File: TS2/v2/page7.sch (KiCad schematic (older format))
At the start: 10 parts, among them P1 FTDI (TERMINAL), P2 FTDI (HOST), U29 6850, U3 74LS00, U30 6850, U31 MC14411, U5 74LS04, Y1 1.842MHz

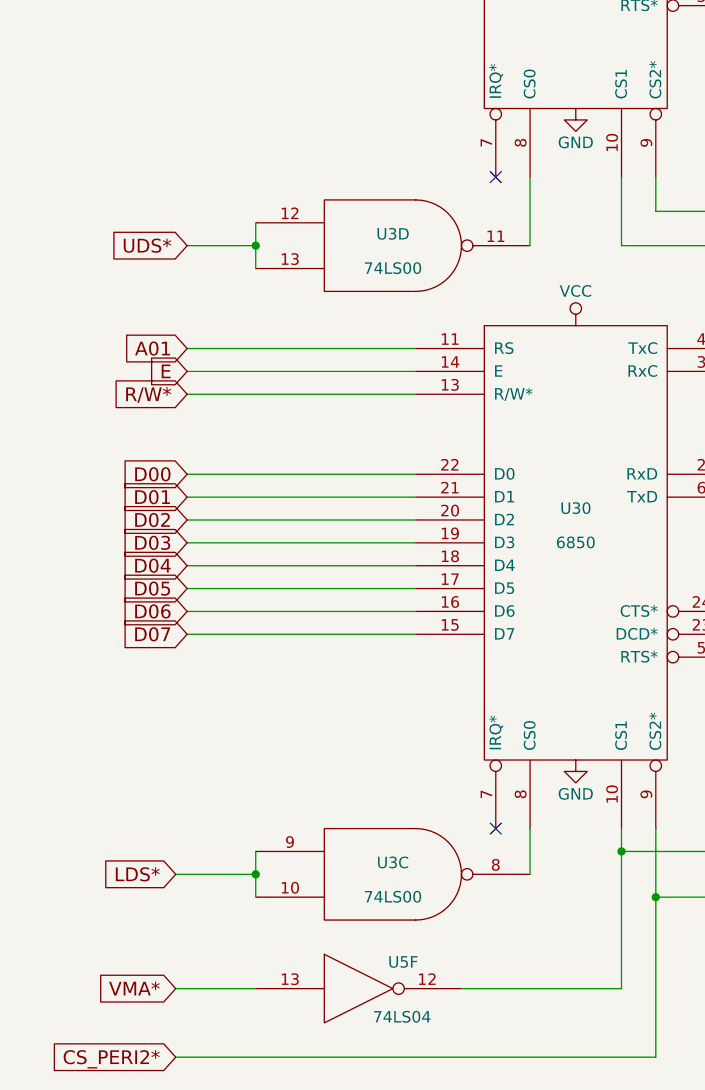
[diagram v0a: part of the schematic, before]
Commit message: Implementing more of interrupt circuitry.
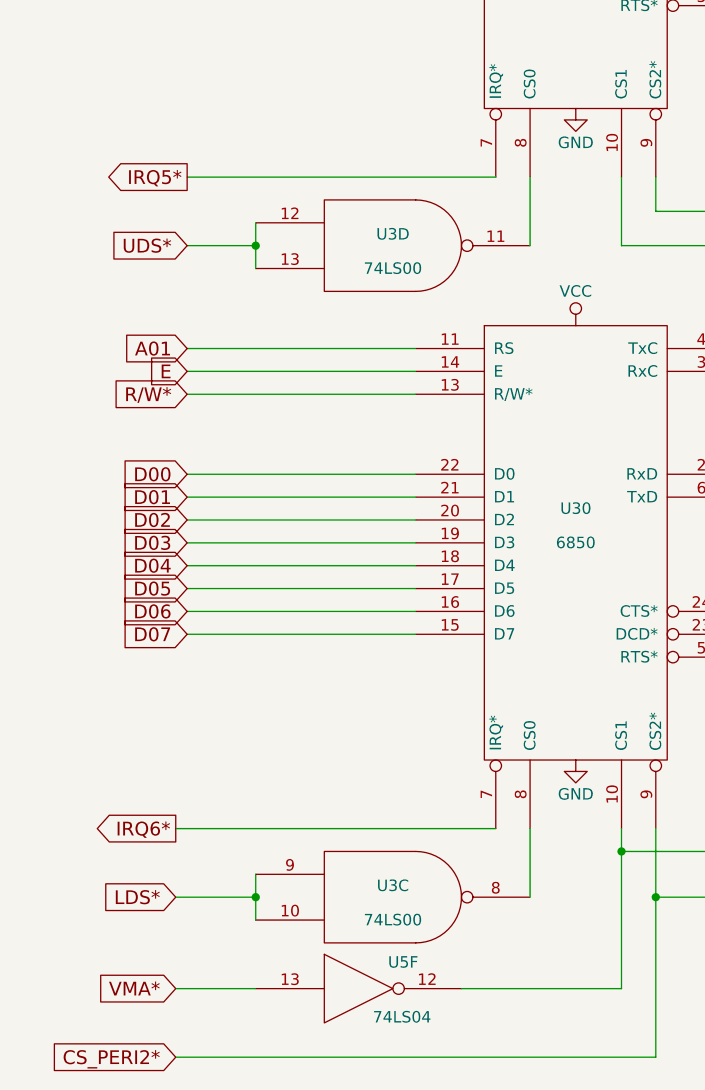
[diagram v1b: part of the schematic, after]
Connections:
- net IRQ5*: now reaches U29.7 (IRQ*)
- net IRQ6*: now reaches U30.7 (IRQ*)
- no-connect marks 12 -> 10
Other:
- moved on the sheet: U3C
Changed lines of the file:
@@
 $EndComp
 $Comp
-L GND #PWR089
+L GND #PWR088
 U 1 1 57C6835F
 P 7250 2050
-F 0 "#PWR089" H 7250 1800 50  0001 C CNN
+F 0 "#PWR088" H 7250 1800 50  0001 C CNN
 F 1 "GND" H 7250 1900 50  0000 C CNN
 F 2 "" H 7250 2050 50  0000 C CNN
@@
 $EndComp
 $Comp
-L VCC #PWR090
+L VCC #PWR089
 U 1 1 57C6838D
 P 7250 1150
-F 0 "#PWR090" H 7250 1000 50  0001 C CNN
+F 0 "#PWR089" H 7250 1000 50  0001 C CNN
 F 1 "VCC" H 7250 1300 50  0000 C CNN
 F 2 "" H 7250 1150 50  0000 C CNN
@@
 $EndComp
 $Comp
-L GND #PWR091
+L GND #PWR090
 U 1 1 57C688B5
 P 6450 1450
-F 0 "#PWR091" H 6450 1200 50  0001 C CNN
+F 0 "#PWR090" H 6450 1200 50  0001 C CNN
 F 1 "GND" H 6450 1300 50  0000 C CNN
 F 2 "" H 6450 1450 50  0000 C CNN
@@
 $EndComp
 $Comp
-L VCC #PWR092
+L VCC #PWR091
 U 1 1 57C688E3
 P 6450 1250
-F 0 "#PWR092" H 6450 1100 50  0001 C CNN
+F 0 "#PWR091" H 6450 1100 50  0001 C CNN
 F 1 "VCC" H 6450 1400 50  0000 C CNN
 F 2 "" H 6450 1250 50  0000 C CNN
@@
 	1    0    0    -1
 $EndComp
-NoConn ~ 3450 3850
-NoConn ~ 3450 6700
-Text GLabel 2050 6900 0    60   Input ~ 0
+Text GLabel 2050 7000 0    60   Input ~ 0
 LDS*
 Text GLabel 2050 7400 0    60   Input ~ 0
@@
 D15
 $Comp
-L VCC #PWR093
+L VCC #PWR092
 U 1 1 57C7A398
 P 3800 1650
-F 0 "#PWR093" H 3800 1500 50  0001 C CNN
+F 0 "#PWR092" H 3800 1500 50  0001 C CNN
 F 1 "VCC" H 3800 1800 50  0000 C CNN
 F 2 "" H 3800 1650 50  0000 C CNN
@@
 $EndComp
 $Comp
-L GND #PWR094
+L GND #PWR093
 U 1 1 57C7A4BC
 P 3800 3550
-F 0 "#PWR094" H 3800 3300 50  0001 C CNN
+F 0 "#PWR093" H 3800 3300 50  0001 C CNN
 F 1 "GND" H 3800 3400 50  0000 C CNN
 F 2 "" H 3800 3550 50  0000 C CNN
@@
 $EndComp
 $Comp
-L VCC #PWR095
+L VCC #PWR094
 U 1 1 57C7A5E0
 P 3800 4500
-F 0 "#PWR095" H 3800 4350 50  0001 C CNN
+F 0 "#PWR094" H 3800 4350 50  0001 C CNN
 F 1 "VCC" H 3800 4650 50  0000 C CNN
 F 2 "" H 3800 4500 50  0000 C CNN
@@
 $EndComp
 $Comp
-L GND #PWR096
+L GND #PWR095
 U 1 1 57C7A616
 P 3800 6400
-F 0 "#PWR096" H 3800 6150 50  0001 C CNN
+F 0 "#PWR095" H 3800 6150 50  0001 C CNN
 F 1 "GND" H 3800 6250 50  0000 C CNN
 F 2 "" H 3800 6400 50  0000 C CNN
@@
 $EndComp
 $Comp
-L GND #PWR097
+L GND #PWR096
 U 1 1 57CB2088
 P 8450 2000
-F 0 "#PWR097" H 8450 1750 50  0001 C CNN
+F 0 "#PWR096" H 8450 1750 50  0001 C CNN
 F 1 "GND" H 8450 1850 50  0000 C CNN
 F 2 "" H 8450 2000 50  0000 C CNN
@@
 $EndComp
 $Comp
-L GND #PWR098
+L GND #PWR097
 U 1 1 57CB2D6B
 P 4500 3000
-F 0 "#PWR098" H 4500 2750 50  0001 C CNN
+F 0 "#PWR097" H 4500 2750 50  0001 C CNN
 F 1 "GND" H 4500 2850 50  0000 C CNN
 F 2 "" H 4500 3000 50  0000 C CNN
@@
 $EndComp
 $Comp
-L GND #PWR099
+L GND #PWR098
 U 1 1 57CB394C
 P 8450 4850
-F 0 "#PWR099" H 8450 4600 50  0001 C CNN
+F 0 "#PWR098" H 8450 4600 50  0001 C CNN
 F 1 "GND" H 8450 4700 50  0000 C CNN
 F 2 "" H 8450 4850 50  0000 C CNN
@@
 $EndComp
 $Comp
-L GND #PWR0100
+L GND #PWR099
 U 1 1 57CB4274
 P 4500 5850
-F 0 "#PWR0100" H 4500 5600 50  0001 C CNN
+F 0 "#PWR099" H 4500 5600 50  0001 C CNN
 F 1 "GND" H 4500 5700 50  0000 C CNN
 F 2 "" H 4500 5850 50  0000 C CNN
@@
 L 74LS00 U3
 U 3 1 5842F0A3
-P 3000 6900
-F 0 "U3" H 3000 6950 50  0000 C CNN
-F 1 "74LS00" H 3000 6800 50  0000 C CNN
-F 2 "" H 3000 6900 50  0000 C CNN
-F 3 "" H 3000 6900 50  0000 C CNN
-	3    3000 6900
+P 3000 7000
+F 0 "U3" H 3000 7050 50  0000 C CNN
+F 1 "74LS00" H 3000 6900 50  0000 C CNN
+F 2 "" H 3000 7000 50  0000 C CNN
+F 3 "" H 3000 7000 50  0000 C CNN
+	3    3000 7000
 	1    0    0    -1
 $EndComp
@@
 $EndComp
 Wire Wire Line
-	3600 6700 3600 6900
-Wire Wire Line
-	2400 6800 2400 7000
-Wire Wire Line
-	2400 6900 2050 6900
-Connection ~ 2400 6900
+	3600 6700 3600 7000
+Wire Wire Line
+	2400 6900 2400 7100
+Wire Wire Line
+	2400 7000 2050 7000
+Connection ~ 2400 7000
 Wire Wire Line
 	4000 6700 4000 7400
@@
 $EndComp
 $Comp
-L VCC #PWR0101
+L VCC #PWR0100
 U 1 1 586F01FE
 P 8200 2100
-F 0 "#PWR0101" H 8200 1950 50  0001 C CNN
+F 0 "#PWR0100" H 8200 1950 50  0001 C CNN
 F 1 "VCC" H 8200 2250 50  0000 C CNN
 F 2 "" H 8200 2100 50  0000 C CNN
@@
 Text Notes 8350 3100 0    60   ~ 0
 Connect jumper JP5 to use optional USB\npower instead of external power supply.
+Text GLabel 2100 3850 0    60   Output ~ 0
+IRQ5*
+Wire Wire Line
+	2100 3850 3450 3850
+Wire Wire Line
+	3450 6700 2050 6700
+Text GLabel 2050 6700 0    60   Output ~ 0
+IRQ6*
 $EndSCHEMATC

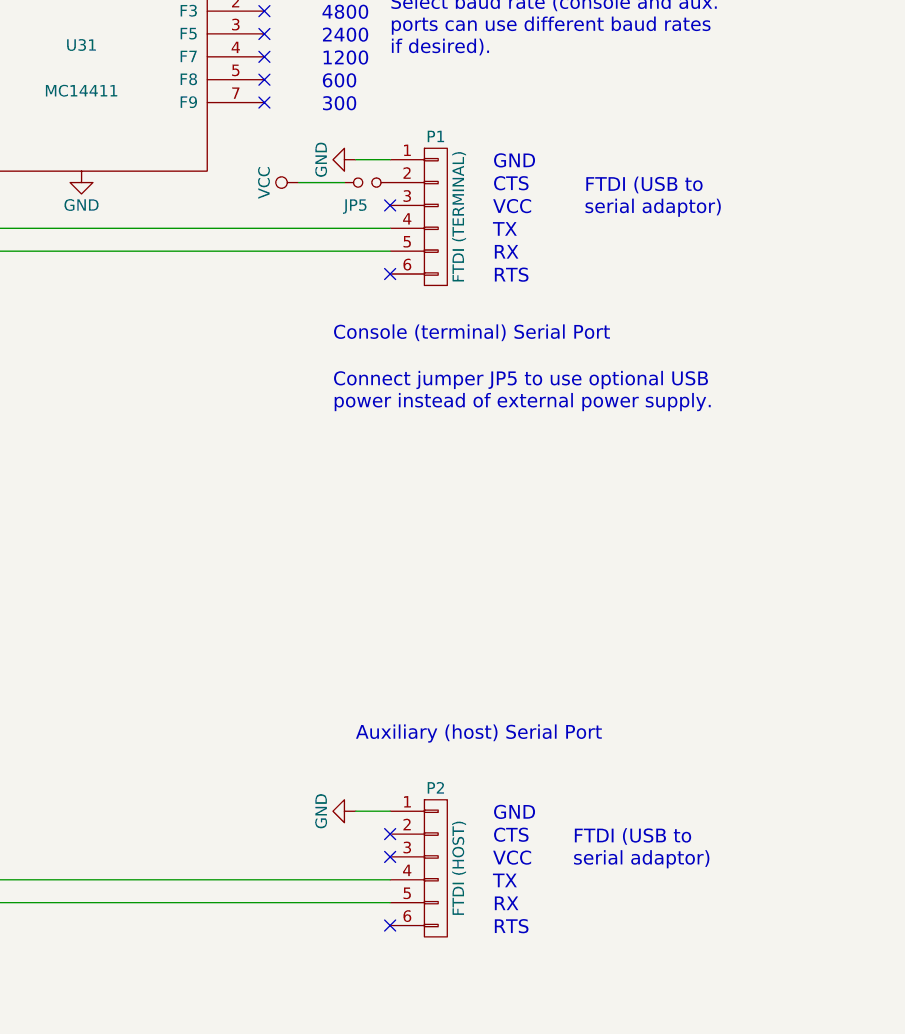
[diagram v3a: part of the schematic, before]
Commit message: Fix up some issues with power supply circuitry.
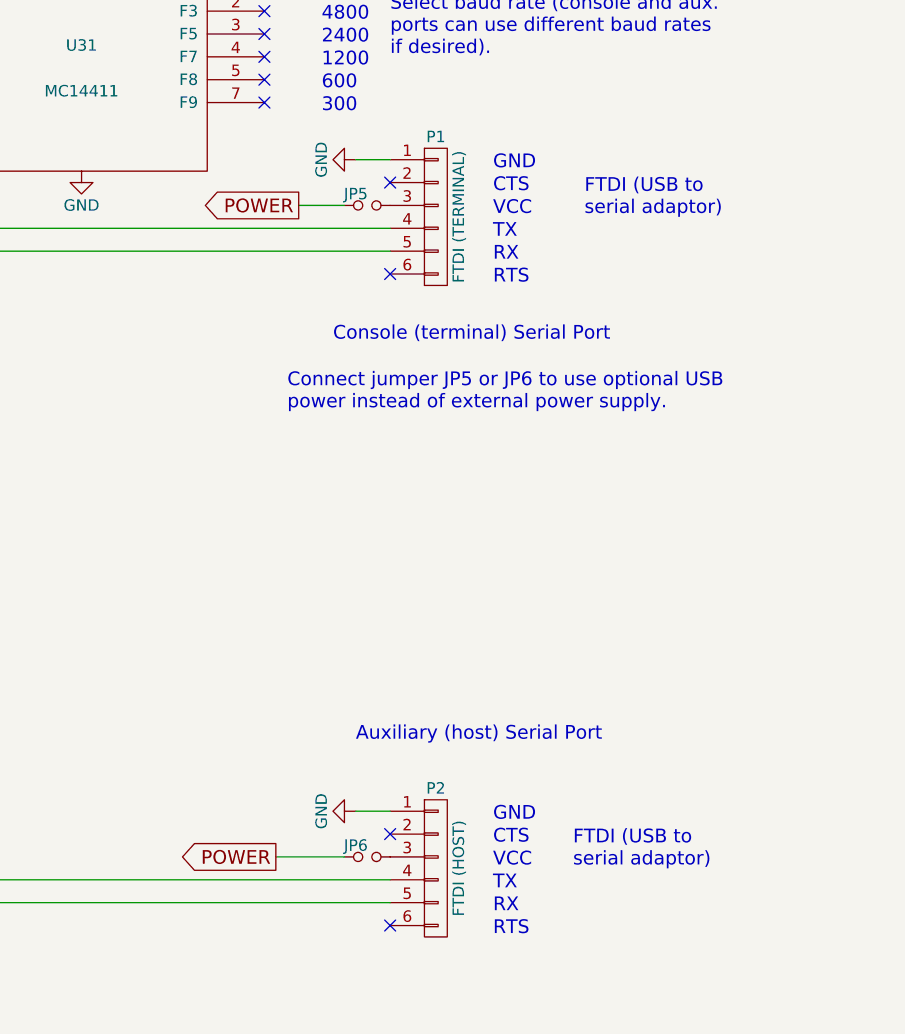
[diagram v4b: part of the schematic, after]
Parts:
- added JP6: Jumper_NO_Small, symbol Jumper_NO_Small
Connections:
- net VCC: no longer JP5.1
- net at P1.2 (P2): no longer JP5.2
- net at P1.3 (P3): now also JP5.2
- net at P2.3 (P3): now also JP6.2
- new net POWER: JP5.1, JP6.1
- no-connect marks 10 -> 9
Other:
- note added: "Connect jumper JP5 or JP6 to use optional USB\npower instead of external power supply."
- note removed: "Connect jumper JP5 to use optional USB\npower instead of external power supply."
- moved on the sheet: JP5
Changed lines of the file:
@@
 Sheet 8 9
 Title "TS2 68000 Single Board Computer"
-Date "2017-01-15"
+Date "2017-01-19"
 Rev "2.0"
 Comp "Jeff Tranter"
@@
 Text Notes 8450 4550 0    60   ~ 0
 Auxiliary (host) Serial Port
-NoConn ~ 8600 2200
-NoConn ~ 8600 5050
+NoConn ~ 8600 2100
 Wire Wire Line
 	5300 800  5300 1850
@@
 L Jumper_NO_Small JP5
 U 1 1 586F01C1
-P 8500 2100
-F 0 "JP5" H 8450 2000 50  0000 C CNN
-F 1 "Jumper_NO_Small" H 8510 2040 50  0001 C CNN
-F 2 "" H 8500 2100 50  0000 C CNN
-F 3 "" H 8500 2100 50  0000 C CNN
-	1    8500 2100
-	1    0    0    -1
-$EndComp
-$Comp
-L VCC #PWR0104
-U 1 1 586F01FE
-P 8200 2100
-F 0 "#PWR0104" H 8200 1950 50  0001 C CNN
-F 1 "VCC" H 8200 2250 50  0000 C CNN
-F 2 "" H 8200 2100 50  0000 C CNN
-F 3 "" H 8200 2100 50  0000 C CNN
-	1    8200 2100
-	0    -1   -1   0
-$EndComp
-Wire Wire Line
-	8200 2100 8400 2100
+P 8500 2200
+F 0 "JP5" H 8450 2250 50  0000 C CNN
+F 1 "Jumper_NO_Small" H 8510 2140 50  0001 C CNN
+F 2 "" H 8500 2200 50  0000 C CNN
+F 3 "" H 8500 2200 50  0000 C CNN
+	1    8500 2200
+	1    0    0    -1
+$EndComp
+Wire Wire Line
+	8200 2200 8400 2200
 Text Notes 8350 2800 0    60   ~ 0
 Console (terminal) Serial Port
-Text Notes 8350 3100 0    60   ~ 0
-Connect jumper JP5 to use optional USB\npower instead of external power supply.
+Text Notes 8150 3100 0    60   ~ 0
+Connect jumper JP5 or JP6 to use optional USB\npower instead of external power supply.
 Text GLabel 2100 3850 0    60   Output ~ 0
 IRQ5*
@@
 Text GLabel 2050 6700 0    60   Output ~ 0
 IRQ6*
+$Comp
+L Jumper_NO_Small JP6
+U 1 1 5880D454
+P 8500 5050
+F 0 "JP6" H 8450 5100 50  0000 C CNN
+F 1 "Jumper_NO_Small" H 8510 4990 50  0001 C CNN
+F 2 "" H 8500 5050 50  0000 C CNN
+F 3 "" H 8500 5050 50  0000 C CNN
+	1    8500 5050
+	1    0    0    -1
+$EndComp
+Wire Wire Line
+	8100 5050 8400 5050
+Text GLabel 8200 2200 0    60   Output ~ 0
+POWER
+Text GLabel 8100 5050 0    60   Output ~ 0
+POWER
 $EndSCHEMATC

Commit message: Add all bypass caps, show pullups as SIP resistors, start PCB layout.
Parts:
- JP5, JP6: footprint (none) -> Buttons_Switches_ThroughHole:SW_DIP_x1_Slide
- P1, P2: footprint (none) -> Connect:PINHEAD1-6
- R20: footprint (none) -> Resistors_ThroughHole:Resistor_Horizontal_RM7mm
- U29, U30, U31: footprint (none) -> Housings_DIP:DIP-24_W7.62mm
- U3, U5: footprint (none) -> Housings_DIP:DIP-14_W7.62mm
- Y1: footprint (none) -> Crystals:Crystal_HC49-U_Vertical
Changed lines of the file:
@@
 Sheet 8 9
 Title "TS2 68000 Single Board Computer"
-Date "2017-01-19"
+Date "2017-01-23"
 Rev "2.0"
 Comp "Jeff Tranter"
@@
 F 0 "U29" H 3800 2800 50  0000 C CNN
 F 1 "6850" H 3800 2650 50  0000 C CNN
-F 2 "" H 3800 2600 50  0000 C CNN
+F 2 "Housings_DIP:DIP-24_W7.62mm" H 3800 2600 50  0001 C CNN
 F 3 "" H 3800 2600 50  0000 C CNN
 	1    3800 2600
@@
 F 0 "U30" H 3800 5600 50  0000 C CNN
 F 1 "6850" H 3800 5450 50  0000 C CNN
-F 2 "" H 3800 5450 50  0000 C CNN
+F 2 "Housings_DIP:DIP-24_W7.62mm" H 3800 5450 50  0001 C CNN
 F 3 "" H 3800 5450 50  0000 C CNN
 	1    3800 5450
@@
 F 0 "U31" H 7250 1700 50  0000 C CNN
 F 1 "MC14411" H 7250 1500 50  0000 C CNN
-F 2 "" H 7250 1600 50  0000 C CNN
+F 2 "Housings_DIP:DIP-24_W7.62mm" H 7250 1600 50  0001 C CNN
 F 3 "" H 7250 1600 50  0000 C CNN
 	1    7250 1600
@@
 F 0 "Y1" H 6350 1950 50  0000 C CNN
 F 1 "1.842MHz" H 6350 1750 50  0000 C CNN
-F 2 "" H 6350 1850 50  0000 C CNN
+F 2 "Crystals:Crystal_HC49-U_Vertical" H 6350 1850 50  0001 C CNN
 F 3 "" H 6350 1850 50  0000 C CNN
 	1    6350 1850
@@
 F 0 "R20" V 6180 1850 50  0000 C CNN
 F 1 "15M" V 6100 1850 50  0000 C CNN
-F 2 "" V 6030 1850 50  0000 C CNN
+F 2 "Resistors_ThroughHole:Resistor_Horizontal_RM7mm" V 6030 1850 50  0001 C CNN
 F 3 "" H 6100 1850 50  0000 C CNN
 	1    6100 1850
@@
 $EndComp
 $Comp
-L GND #PWR092
+L GND #PWR094
 U 1 1 57C6835F
 P 7250 2050
-F 0 "#PWR092" H 7250 1800 50  0001 C CNN
+F 0 "#PWR094" H 7250 1800 50  0001 C CNN
 F 1 "GND" H 7250 1900 50  0000 C CNN
 F 2 "" H 7250 2050 50  0000 C CNN
@@
 $EndComp
 $Comp
-L VCC #PWR093
+L VCC #PWR095
 U 1 1 57C6838D
 P 7250 1150
-F 0 "#PWR093" H 7250 1000 50  0001 C CNN
+F 0 "#PWR095" H 7250 1000 50  0001 C CNN
 F 1 "VCC" H 7250 1300 50  0000 C CNN
 F 2 "" H 7250 1150 50  0000 C CNN
@@
 $EndComp
 $Comp
-L GND #PWR094
+L GND #PWR096
 U 1 1 57C688B5
 P 6450 1450
-F 0 "#PWR094" H 6450 1200 50  0001 C CNN
+F 0 "#PWR096" H 6450 1200 50  0001 C CNN
 F 1 "GND" H 6450 1300 50  0000 C CNN
 F 2 "" H 6450 1450 50  0000 C CNN
@@
 $EndComp
 $Comp
-L VCC #PWR095
+L VCC #PWR097
 U 1 1 57C688E3
 P 6450 1250
-F 0 "#PWR095" H 6450 1100 50  0001 C CNN
+F 0 "#PWR097" H 6450 1100 50  0001 C CNN
 F 1 "VCC" H 6450 1400 50  0000 C CNN
 F 2 "" H 6450 1250 50  0000 C CNN
@@
 F 0 "U5" H 3045 7515 50  0000 C CNN
 F 1 "74LS04" H 3040 7275 50  0000 C CNN
-F 2 "" H 2850 7400 50  0000 C CNN
+F 2 "Housings_DIP:DIP-14_W7.62mm" H 2850 7400 50  0001 C CNN
 F 3 "" H 2850 7400 50  0000 C CNN
 	6    2850 7400
@@
 D15
 $Comp
-L VCC #PWR096
+L VCC #PWR098
 U 1 1 57C7A398
 P 3800 1650
-F 0 "#PWR096" H 3800 1500 50  0001 C CNN
+F 0 "#PWR098" H 3800 1500 50  0001 C CNN
 F 1 "VCC" H 3800 1800 50  0000 C CNN
 F 2 "" H 3800 1650 50  0000 C CNN
@@
 $EndComp
 $Comp
-L GND #PWR097
+L GND #PWR099
 U 1 1 57C7A4BC
 P 3800 3550
-F 0 "#PWR097" H 3800 3300 50  0001 C CNN
+F 0 "#PWR099" H 3800 3300 50  0001 C CNN
 F 1 "GND" H 3800 3400 50  0000 C CNN
 F 2 "" H 3800 3550 50  0000 C CNN
@@
 $EndComp
 $Comp
-L VCC #PWR098
+L VCC #PWR0100
 U 1 1 57C7A5E0
 P 3800 4500
-F 0 "#PWR098" H 3800 4350 50  0001 C CNN
+F 0 "#PWR0100" H 3800 4350 50  0001 C CNN
 F 1 "VCC" H 3800 4650 50  0000 C CNN
 F 2 "" H 3800 4500 50  0000 C CNN
@@
 $EndComp
 $Comp
-L GND #PWR099
+L GND #PWR0101
 U 1 1 57C7A616
 P 3800 6400
-F 0 "#PWR099" H 3800 6150 50  0001 C CNN
+F 0 "#PWR0101" H 3800 6150 50  0001 C CNN
 F 1 "GND" H 3800 6250 50  0000 C CNN
 F 2 "" H 3800 6400 50  0000 C CNN
@@
 F 0 "P1" H 8800 2600 50  0000 C CNN
 F 1 "FTDI (TERMINAL)" V 8900 2250 50  0000 C CNN
-F 2 "" H 8800 2250 50  0000 C CNN
+F 2 "Connect:PINHEAD1-6" H 8800 2250 50  0001 C CNN
 F 3 "" H 8800 2250 50  0000 C CNN
 	1    8800 2250
@@
 F 0 "P2" H 8800 5450 50  0000 C CNN
 F 1 "FTDI (HOST)" V 8900 5100 50  0000 C CNN
-F 2 "" H 8800 5100 50  0000 C CNN
+F 2 "Connect:PINHEAD1-6" H 8800 5100 50  0001 C CNN
 F 3 "" H 8800 5100 50  0000 C CNN
 	1    8800 5100
@@
 $EndComp
 $Comp
-L GND #PWR0100
+L GND #PWR0102
 U 1 1 57CB2088
 P 8450 2000
-F 0 "#PWR0100" H 8450 1750 50  0001 C CNN
+F 0 "#PWR0102" H 8450 1750 50  0001 C CNN
 F 1 "GND" H 8450 1850 50  0000 C CNN
 F 2 "" H 8450 2000 50  0000 C CNN
@@
 $EndComp
 $Comp
-L GND #PWR0101
+L GND #PWR0103
 U 1 1 57CB2D6B
 P 4500 3000
-F 0 "#PWR0101" H 4500 2750 50  0001 C CNN
+F 0 "#PWR0103" H 4500 2750 50  0001 C CNN
 F 1 "GND" H 4500 2850 50  0000 C CNN
 F 2 "" H 4500 3000 50  0000 C CNN
@@
 $EndComp
 $Comp
-L GND #PWR0102
+L GND #PWR0104
 U 1 1 57CB394C
 P 8450 4850
-F 0 "#PWR0102" H 8450 4600 50  0001 C CNN
+F 0 "#PWR0104" H 8450 4600 50  0001 C CNN
 F 1 "GND" H 8450 4700 50  0000 C CNN
 F 2 "" H 8450 4850 50  0000 C CNN
@@
 $EndComp
 $Comp
-L GND #PWR0103
+L GND #PWR0105
 U 1 1 57CB4274
 P 4500 5850
-F 0 "#PWR0103" H 4500 5600 50  0001 C CNN
+F 0 "#PWR0105" H 4500 5600 50  0001 C CNN
 F 1 "GND" H 4500 5700 50  0000 C CNN
 F 2 "" H 4500 5850 50  0000 C CNN
@@
 F 0 "U3" H 3000 7050 50  0000 C CNN
 F 1 "74LS00" H 3000 6900 50  0000 C CNN
-F 2 "" H 3000 7000 50  0000 C CNN
+F 2 "Housings_DIP:DIP-14_W7.62mm" H 3000 7000 50  0001 C CNN
 F 3 "" H 3000 7000 50  0000 C CNN
 	3    3000 7000
@@
 F 0 "U3" H 3000 4200 50  0000 C CNN
 F 1 "74LS00" H 3000 4050 50  0000 C CNN
-F 2 "" H 3000 4150 50  0000 C CNN
+F 2 "Housings_DIP:DIP-14_W7.62mm" H 3000 4150 50  0001 C CNN
 F 3 "" H 3000 4150 50  0000 C CNN
 	4    3000 4150
@@
 F 0 "JP5" H 8450 2250 50  0000 C CNN
 F 1 "Jumper_NO_Small" H 8510 2140 50  0001 C CNN
-F 2 "" H 8500 2200 50  0000 C CNN
+F 2 "Buttons_Switches_ThroughHole:SW_DIP_x1_Slide" H 8500 2200 50  0001 C CNN
 F 3 "" H 8500 2200 50  0000 C CNN
 	1    8500 2200
@@
 F 0 "JP6" H 8450 5100 50  0000 C CNN
 F 1 "Jumper_NO_Small" H 8510 4990 50  0001 C CNN
-F 2 "" H 8500 5050 50  0000 C CNN
+F 2 "Buttons_Switches_ThroughHole:SW_DIP_x1_Slide" H 8500 5050 50  0001 C CNN
 F 3 "" H 8500 5050 50  0000 C CNN
 	1    8500 5050

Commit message: Working on PCB layout.
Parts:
- JP5, JP6: footprint Buttons_Switches_ThroughHole:SW_DIP_x1_Slide -> Connect:PINHEAD1-2
- U29, U30, U31: footprint Housings_DIP:DIP-24_W7.62mm -> Housings_DIP:DIP-24_W15.24mm
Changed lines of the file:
@@
 F 0 "U29" H 3800 2800 50  0000 C CNN
 F 1 "6850" H 3800 2650 50  0000 C CNN
-F 2 "Housings_DIP:DIP-24_W7.62mm" H 3800 2600 50  0001 C CNN
+F 2 "Housings_DIP:DIP-24_W15.24mm" H 3800 2600 50  0001 C CNN
 F 3 "" H 3800 2600 50  0000 C CNN
 	1    3800 2600
@@
 F 0 "U30" H 3800 5600 50  0000 C CNN
 F 1 "6850" H 3800 5450 50  0000 C CNN
-F 2 "Housings_DIP:DIP-24_W7.62mm" H 3800 5450 50  0001 C CNN
+F 2 "Housings_DIP:DIP-24_W15.24mm" H 3800 5450 50  0001 C CNN
 F 3 "" H 3800 5450 50  0000 C CNN
 	1    3800 5450
@@
 F 0 "U31" H 7250 1700 50  0000 C CNN
 F 1 "MC14411" H 7250 1500 50  0000 C CNN
-F 2 "Housings_DIP:DIP-24_W7.62mm" H 7250 1600 50  0001 C CNN
+F 2 "Housings_DIP:DIP-24_W15.24mm" H 7250 1600 50  0001 C CNN
 F 3 "" H 7250 1600 50  0000 C CNN
 	1    7250 1600
@@
 F 0 "JP5" H 8450 2250 50  0000 C CNN
 F 1 "Jumper_NO_Small" H 8510 2140 50  0001 C CNN
-F 2 "Buttons_Switches_ThroughHole:SW_DIP_x1_Slide" H 8500 2200 50  0001 C CNN
+F 2 "Connect:PINHEAD1-2" H 8500 2200 50  0001 C CNN
 F 3 "" H 8500 2200 50  0000 C CNN
 	1    8500 2200
@@
 F 0 "JP6" H 8450 5100 50  0000 C CNN
 F 1 "Jumper_NO_Small" H 8510 4990 50  0001 C CNN
-F 2 "Buttons_Switches_ThroughHole:SW_DIP_x1_Slide" H 8500 5050 50  0001 C CNN
+F 2 "Connect:PINHEAD1-2" H 8500 5050 50  0001 C CNN
 F 3 "" H 8500 5050 50  0000 C CNN
 	1    8500 5050
